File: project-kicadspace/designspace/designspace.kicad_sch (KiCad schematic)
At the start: 18 parts, among them IC1 ADE7758, U1 STM32F103C8Tx

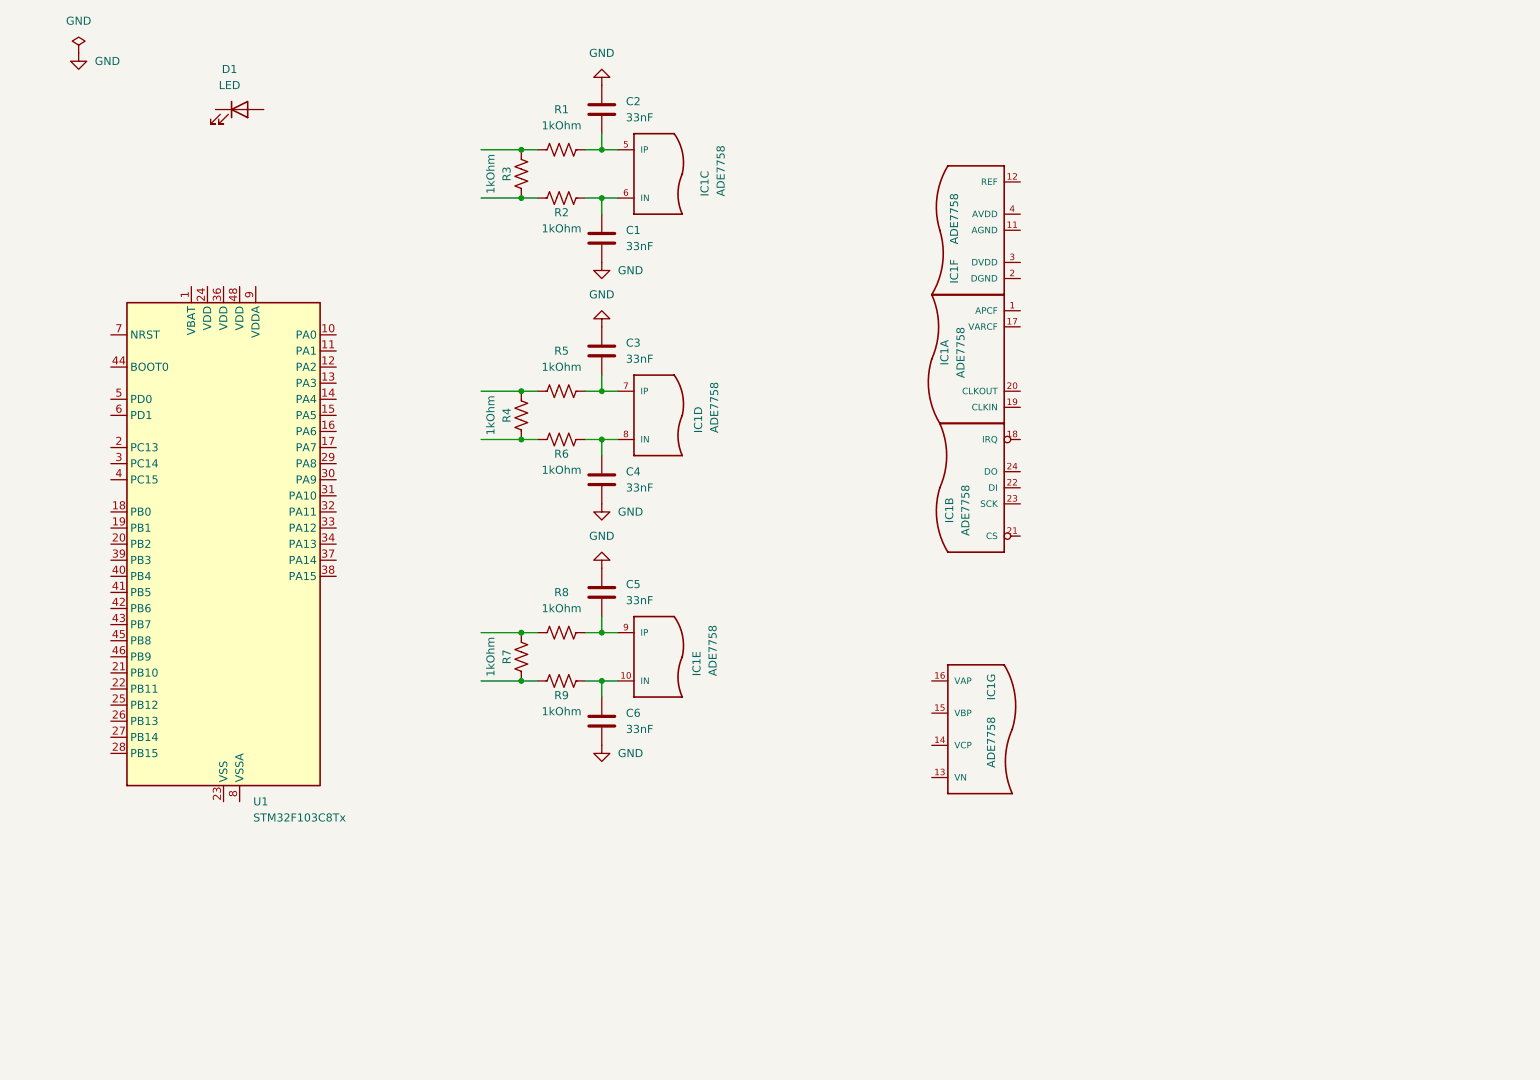
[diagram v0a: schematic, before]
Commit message: feat(pcb): implement test circuit for ade7758
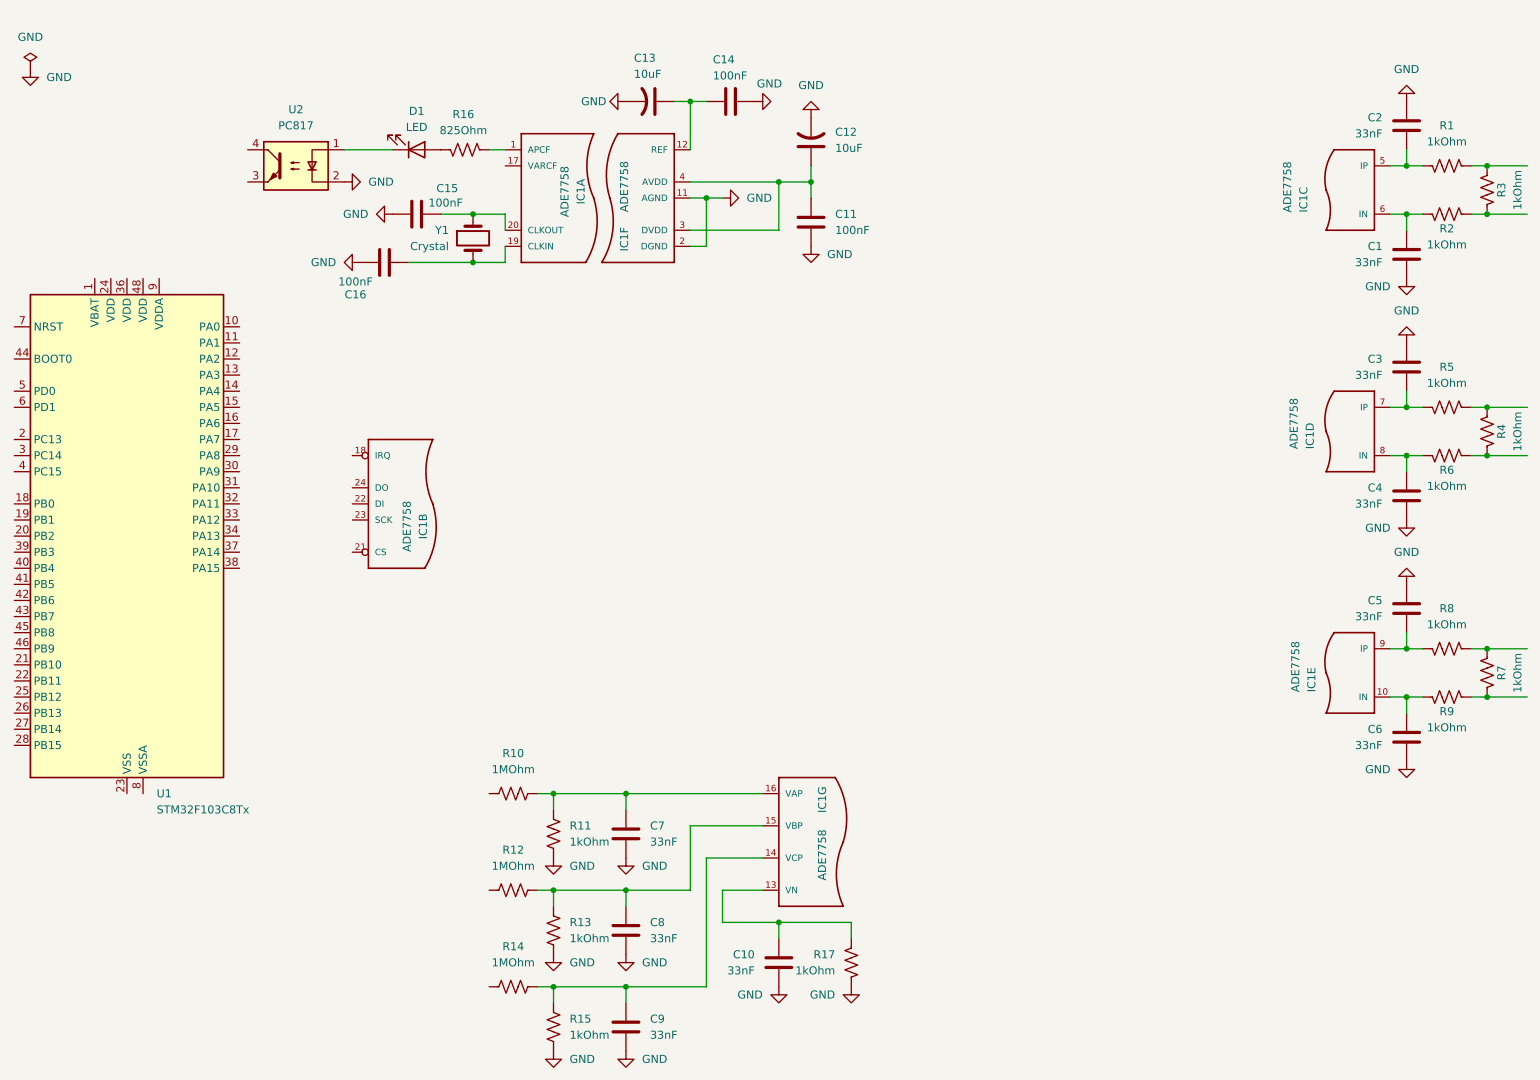
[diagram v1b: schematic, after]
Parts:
- added C10, C7, C8, C9: 33nF, symbol Device:C
- added C11, C14, C15, C16: 100nF, symbol Device:C
- added C12, C13: 10uF, symbol Device:C_US
- added R10, R12, R14: 1MOhm, symbol Device:R_US
- added R11, R13, R15, R17: 1kOhm, symbol Device:R_US
- added R16: 825Ohm, symbol Device:R_US
- added U2: PC817, Package_DIP:DIP-4_W7.62mm, symbol Isolator:PC817
- added Y1: Crystal, symbol Device:Crystal
- U1: footprint Package_QFP:LQFP-48_7x7mm_P0.5mm -> BluePill_breakouts:BluePill_STM32F103C
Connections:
- net GND: now also IC1.11 (AGND), IC1.2 (DGND), C10.2, C11.2, C12.2, C13.2, C14.2, C15.1, C16.2, C7.2, C8.2, C9.2, R11.2, R13.2, R15.2, R17.2, U2.2
- net at IC1.13 (VN): now also C10.1, R17.1
- net at IC1.14 (VCP): now also C9.1, R14.1, R15.1
- net at IC1.15 (VBP): now also C8.1, R12.1, R13.1
- net at IC1.16 (VAP): now also C7.1, R10.1, R11.1
- net at D1.1 (K): now also U2.1
- net at D1.2 (A): now also R16.1
- net at IC1.1 (APCF): now also R16.2
- net at IC1.19 (CLKIN): now also C16.1, Y1.2
- net at IC1.20 (CLKOUT): now also C15.2, Y1.1
- net at IC1.12 (REF): now also C13.1, C14.1
- net at IC1.3 (DVDD): now also IC1.4 (AVDD), C11.1, C12.1
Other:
- moved on the sheet: C1, C2, C3, C4, C5, C6, D1, IC1A, IC1B, IC1C, IC1D, IC1E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
